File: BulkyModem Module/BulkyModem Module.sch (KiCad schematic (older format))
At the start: 13 parts, among them M1 Mounting, M2 Mounting, M3 Mounting, M4 Mounting, U1 74HCT244, U2 74HCT04

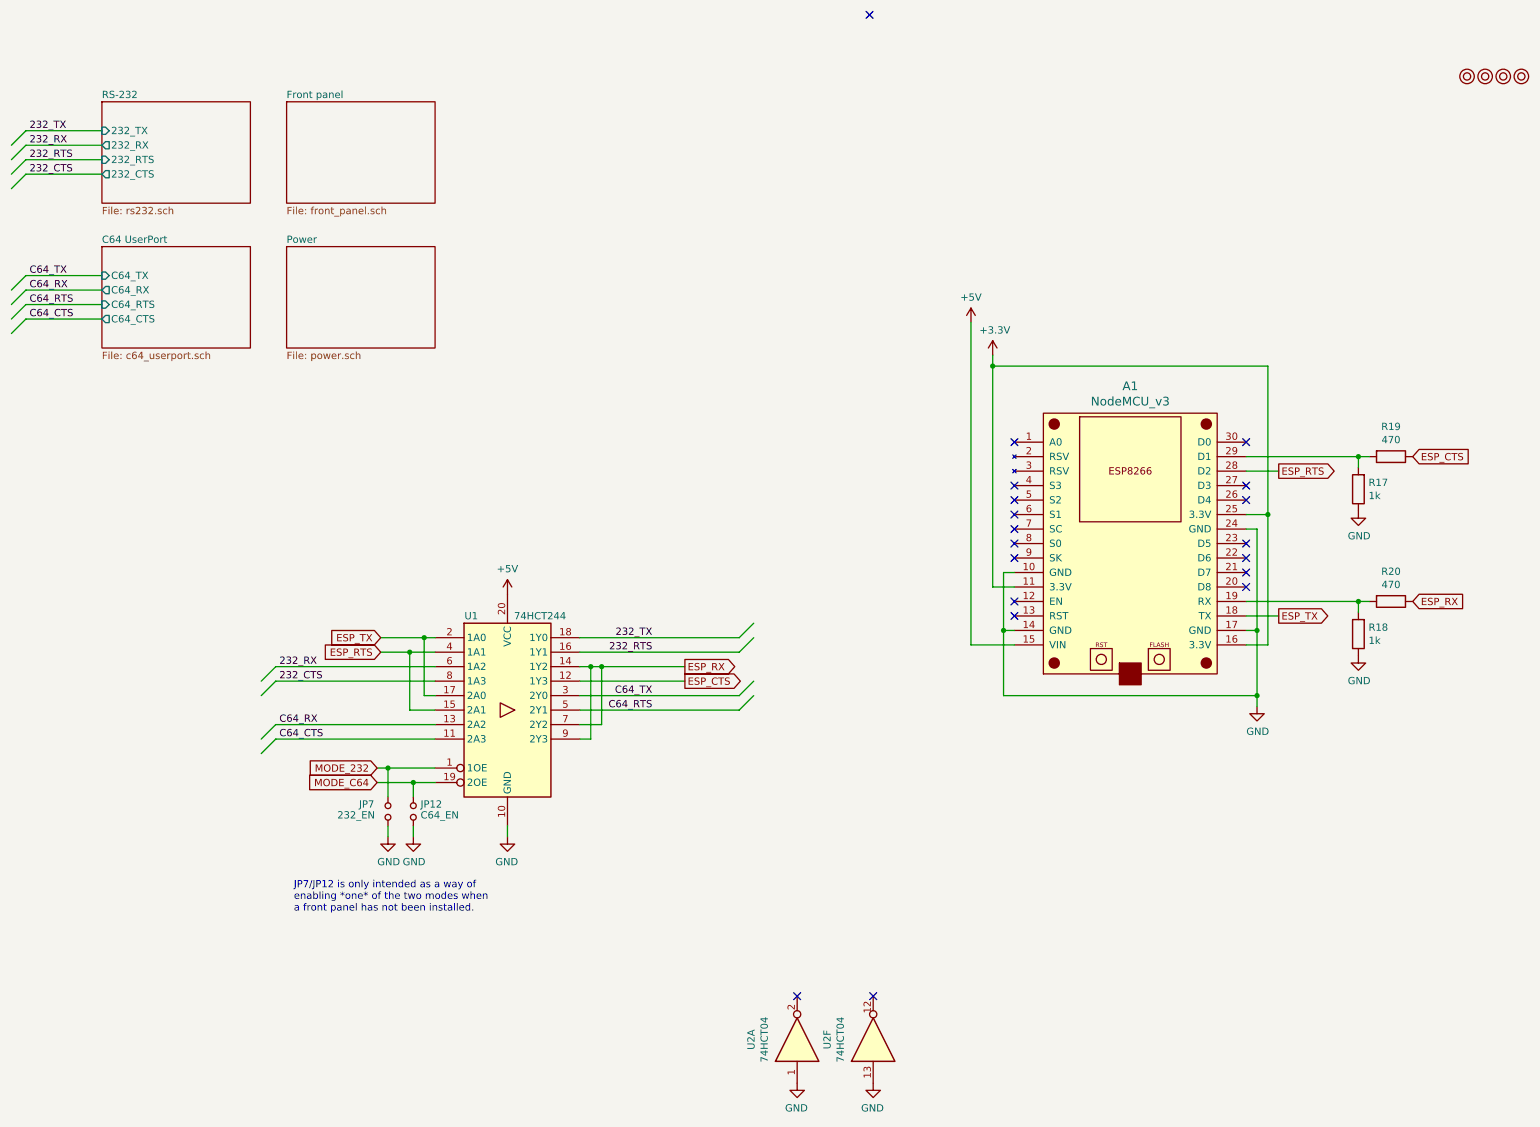
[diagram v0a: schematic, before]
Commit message: C64 UserPort adapter sketched out (preliminary layout)
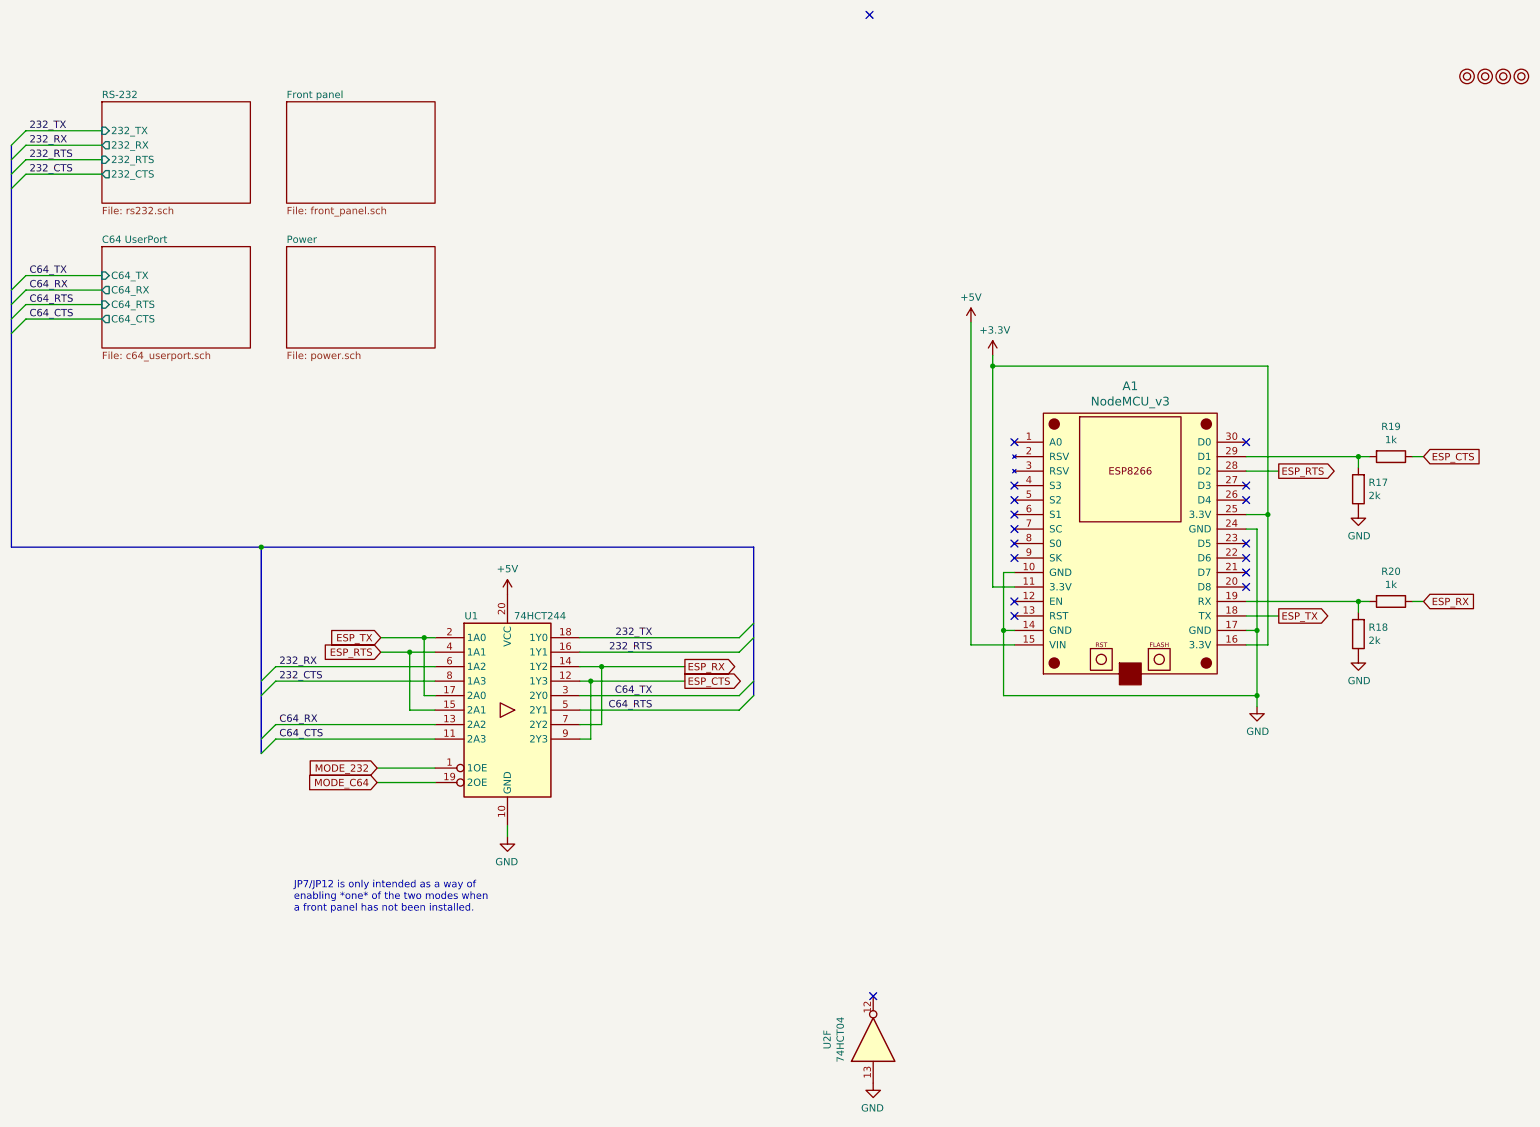
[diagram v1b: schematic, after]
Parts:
- removed JP12: C64_EN, symbol Device:Jumper_NO_Small
- removed JP7: 232_EN, symbol Device:Jumper_NO_Small
- removed unit 1 of U2
- R17, R18: value 1k -> 2k; footprint (none) -> resistor:R_Axial_DIN0207_L6.3mm_D2.5mm_P10.16mm_Horizontal
- R19, R20: value 470 -> 1k; footprint (none) -> resistor:R_Axial_DIN0207_L6.3mm_D2.5mm_P10.16mm_Horizontal
- U1: footprint (none) -> Package_DIP:DIP-20_W7.62mm_Socket_LongPads
- U2: footprint (none) -> Package_DIP:DIP-14_W7.62mm_Socket_LongPads
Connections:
- net ESP_CTS: now also U1.9 (2Y3)
- net ESP_RX: no longer U1.9 (2Y3)
- no-connect marks 19 -> 18
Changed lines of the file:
@@
 F 0 "A1" H 8425 4887 60  0000 C CNN
 F 1 "NodeMCU_v3" H 8425 4781 60  0000 C CNN
-F 2 "" H 7825 2950 60  0000 C CNN
+F 2 "" H 7825 2950 60  0001 C CNN
 F 3 "" H 7825 2950 60  0000 C CNN
 	1    8425 3800
@@
 Wire Wire Line
 	9225 4300 9450 4300
-Text GLabel 10375 4200 2    50   Input ~ 0
+Text GLabel 10450 4200 2    50   Input ~ 0
 ESP_RX
 $Comp
@@
 F 0 "U1" H 3875 5600 50  0000 C CNN
 F 1 "74HCT244" H 4350 5600 50  0000 C CNN
-F 2 "" H 4125 4950 50  0001 C CNN
+F 2 "Package_DIP:DIP-20_W7.62mm_Socket_LongPads" H 4125 4950 50  0001 C CNN
 F 3 "https://assets.nexperia.com/documents/data-sheet/74HC_HCT244.pdf" H 4125 4950 50  0001 C CNN
 	1    4125 4950
@@
 $Comp
 L 74xx:74HCT04 U2
-U 1 1 62F91C25
-P 6125 7225
-F 0 "U2" H 6125 7542 50  0000 C CNN
-F 1 "74HCT04" H 6125 7451 50  0000 C CNN
-F 2 "" H 6125 7225 50  0001 C CNN
-F 3 "https://assets.nexperia.com/documents/data-sheet/74HC_HCT04.pdf" H 6125 7225 50  0001 C CNN
-	1    6125 7225
-	0    -1   -1   0
-$EndComp
-$Comp
-L 74xx:74HCT04 U2
 U 6 1 62F95922
 P 6650 7225
 F 0 "U2" H 6650 7542 50  0000 C CNN
 F 1 "74HCT04" H 6650 7451 50  0000 C CNN
-F 2 "" H 6650 7225 50  0001 C CNN
+F 2 "Package_DIP:DIP-14_W7.62mm_Socket_LongPads" H 6650 7225 50  0001 C CNN
 F 3 "https://assets.nexperia.com/documents/data-sheet/74HC_HCT04.pdf" H 6650 7225 50  0001 C CNN
 	6    6650 7225
 	0    -1   -1   0
 $EndComp
-Text GLabel 10375 3200 2    50   Input ~ 0
+Text GLabel 10450 3200 2    50   Input ~ 0
 ESP_CTS
 Text GLabel 9450 3300 2    50   Output ~ 0
@@
 	9225 3300 9450 3300
 NoConn ~ 6650 6925
-NoConn ~ 6125 6925
 $Sheet
 S 1325 750  1025 700
@@
 	2525 5150 3625 5150
 Wire Wire Line
-	4625 4750 5350 4750
-Wire Wire Line
-	4625 4650 4700 4650
-Wire Wire Line
-	4700 4650 4700 5150
+	4625 4750 4700 4750
 Wire Wire Line
 	4625 5150 4700 5150
-Connection ~ 4700 4650
-Wire Wire Line
-	4775 5050 4775 4650
-Connection ~ 4775 4650
-Wire Wire Line
-	4775 4650 5350 4650
-Wire Wire Line
-	4700 4650 4775 4650
 Wire Wire Line
 	4625 5050 4775 5050
@@
 AR Path="/63E1B523" Ref="R19"  Part="1"
 F 0 "R19" V 10018 3200 50  0000 C CNN
-F 1 "470" V 10109 3200 50  0000 C CNN
-F 2 "" V 10155 3200 50  0001 C CNN
+F 1 "1k" V 10109 3200 50  0000 C CNN
+F 2 "resistor:R_Axial_DIN0207_L6.3mm_D2.5mm_P10.16mm_Horizontal" V 10155 3200 50  0001 C CNN
 F 3 "~" H 10225 3200 50  0001 C CNN
 	1    10225 3200
@@
 AR Path="/63E1D8A2" Ref="R20"  Part="1"
 F 0 "R20" V 10018 4200 50  0000 C CNN
-F 1 "470" V 10109 4200 50  0000 C CNN
-F 2 "" V 10155 4200 50  0001 C CNN
+F 1 "1k" V 10109 4200 50  0000 C CNN
+F 2 "resistor:R_Axial_DIN0207_L6.3mm_D2.5mm_P10.16mm_Horizontal" V 10155 4200 50  0001 C CNN
 F 3 "~" H 10225 4200 50  0001 C CNN
 	1    10225 4200
@@
 AR Path="/63E1DF8E" Ref="R17"  Part="1"
 F 0 "R17" H 9930 3379 50  0000 R CNN
-F 1 "1k" H 9930 3470 50  0000 R CNN
-F 2 "" V 9930 3425 50  0001 C CNN
+F 1 "2k" H 9930 3470 50  0000 R CNN
+F 2 "resistor:R_Axial_DIN0207_L6.3mm_D2.5mm_P10.16mm_Horizontal" V 9930 3425 50  0001 C CNN
 F 3 "~" H 10000 3425 50  0001 C CNN
 	1    10000 3425
@@
 AR Path="/63E2105A" Ref="R18"  Part="1"
 F 0 "R18" H 9930 4379 50  0000 R CNN
-F 1 "1k" H 9930 4470 50  0000 R CNN
-F 2 "" V 9930 4425 50  0001 C CNN
+F 1 "2k" H 9930 4470 50  0000 R CNN
+F 2 "resistor:R_Axial_DIN0207_L6.3mm_D2.5mm_P10.16mm_Horizontal" V 9930 4425 50  0001 C CNN
 F 3 "~" H 10000 4425 50  0001 C CNN
 	1    10000 4425
@@
 $EndComp
 Wire Wire Line
-	3475 5750 3475 5825
-$Comp
-L Device:Jumper_NO_Small JP12
-U 1 1 63E334A2
-P 3475 5650
-AR Path="/63E334A2" Ref="JP12"  Part="1"
-AR Path="/63D786E4/63E334A2" Ref="JP?"  Part="1"
-F 0 "JP12" V 3525 5600 50  0000 R CNN
-F 1 "C64_EN" V 3450 5600 50  0000 R CNN
-F 2 "" H 3475 5650 50  0001 C CNN
-F 3 "~" H 3475 5650 50  0001 C CNN
-	1    3475 5650
-	0    -1   -1   0
-$EndComp
-Wire Wire Line
-	3300 5750 3300 5825
-$Comp
-L Device:Jumper_NO_Small JP7
-U 1 1 63E3925D
-P 3300 5650
-AR Path="/63E3925D" Ref="JP7"  Part="1"
-AR Path="/63D786E4/63E3925D" Ref="JP?"  Part="1"
-F 0 "JP7" V 3350 5850 50  0000 R CNN
-F 1 "232_EN" V 3275 6000 50  0000 R CNN
-F 2 "" H 3300 5650 50  0001 C CNN
-F 3 "~" H 3300 5650 50  0001 C CNN
-	1    3300 5650
-	0    -1   -1   0
-$EndComp
-$Comp
-L power:GND #PWR04
-U 1 1 63E3349C
-P 3475 5825
-AR Path="/63E3349C" Ref="#PWR04"  Part="1"
-AR Path="/63D786E4/63E3349C" Ref="#PWR?"  Part="1"
-F 0 "#PWR04" H 3475 5575 50  0001 C CNN
-F 1 "GND" H 3480 5652 50  0000 C CNN
-F 2 "" H 3475 5825 50  0001 C CNN
-F 3 "" H 3475 5825 50  0001 C CNN
-	1    3475 5825
-	1    0    0    -1
-$EndComp
-$Comp
-L power:GND #PWR02
-U 1 1 63E39257
-P 3300 5825
-AR Path="/63E39257" Ref="#PWR02"  Part="1"
-AR Path="/63D786E4/63E39257" Ref="#PWR?"  Part="1"
-F 0 "#PWR02" H 3300 5575 50  0001 C CNN
-F 1 "GND" H 3305 5652 50  0000 C CNN
-F 2 "" H 3300 5825 50  0001 C CNN
-F 3 "" H 3300 5825 50  0001 C CNN
-	1    3300 5825
-	1    0    0    -1
-$EndComp
-Wire Wire Line
 	4125 5825 4125 5750
-Wire Wire Line
-	3300 5550 3300 5350
-Wire Wire Line
-	3300 5350 3625 5350
-Wire Wire Line
-	3225 5350 3300 5350
-Connection ~ 3300 5350
-Wire Wire Line
-	3225 5450 3475 5450
-Wire Wire Line
-	3475 5450 3475 5550
-Connection ~ 3475 5450
-Wire Wire Line
-	3475 5450 3625 5450
-$Comp
-L power:GND #PWR0137
-U 1 1 63E5BB2D
-P 6125 7525
-F 0 "#PWR0137" H 6125 7275 50  0001 C CNN
-F 1 "GND" H 6130 7352 50  0000 C CNN
-F 2 "" H 6125 7525 50  0001 C CNN
-F 3 "" H 6125 7525 50  0001 C CNN
-	1    6125 7525
-	-1   0    0    -1
-$EndComp
 $Comp
 L power:GND #PWR0138
@@
 Text Notes 2650 6350 0    50   ~ 0
 JP7/JP12 is only intended as a way of\nenabling *one* of the two modes when\na front panel has not been installed.
+Wire Wire Line
+	4625 4650 4775 4650
+Wire Wire Line
+	4700 5150 4700 4750
+Connection ~ 4700 4750
+Wire Wire Line
+	4700 4750 5350 4750
+Wire Wire Line
+	4775 5050 4775 4650
+Connection ~ 4775 4650
+Wire Wire Line
+	4775 4650 5350 4650
+Wire Bus Line
+	2425 3825 5825 3825
+Wire Bus Line
+	700  3825 2425 3825
+Connection ~ 2425 3825
+Wire Wire Line
+	3225 5450 3625 5450
+Wire Wire Line
+	3225 5350 3625 5350
+Wire Wire Line
+	10450 4200 10375 4200
+Wire Wire Line
+	10375 3200 10450 3200
+Wire Bus Line
+	2425 3825 2425 5250
+Wire Bus Line
+	5825 3825 5825 4850
+Wire Bus Line
+	700  1050 700  3825
 $EndSCHEMATC

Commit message: Add MCU footprints
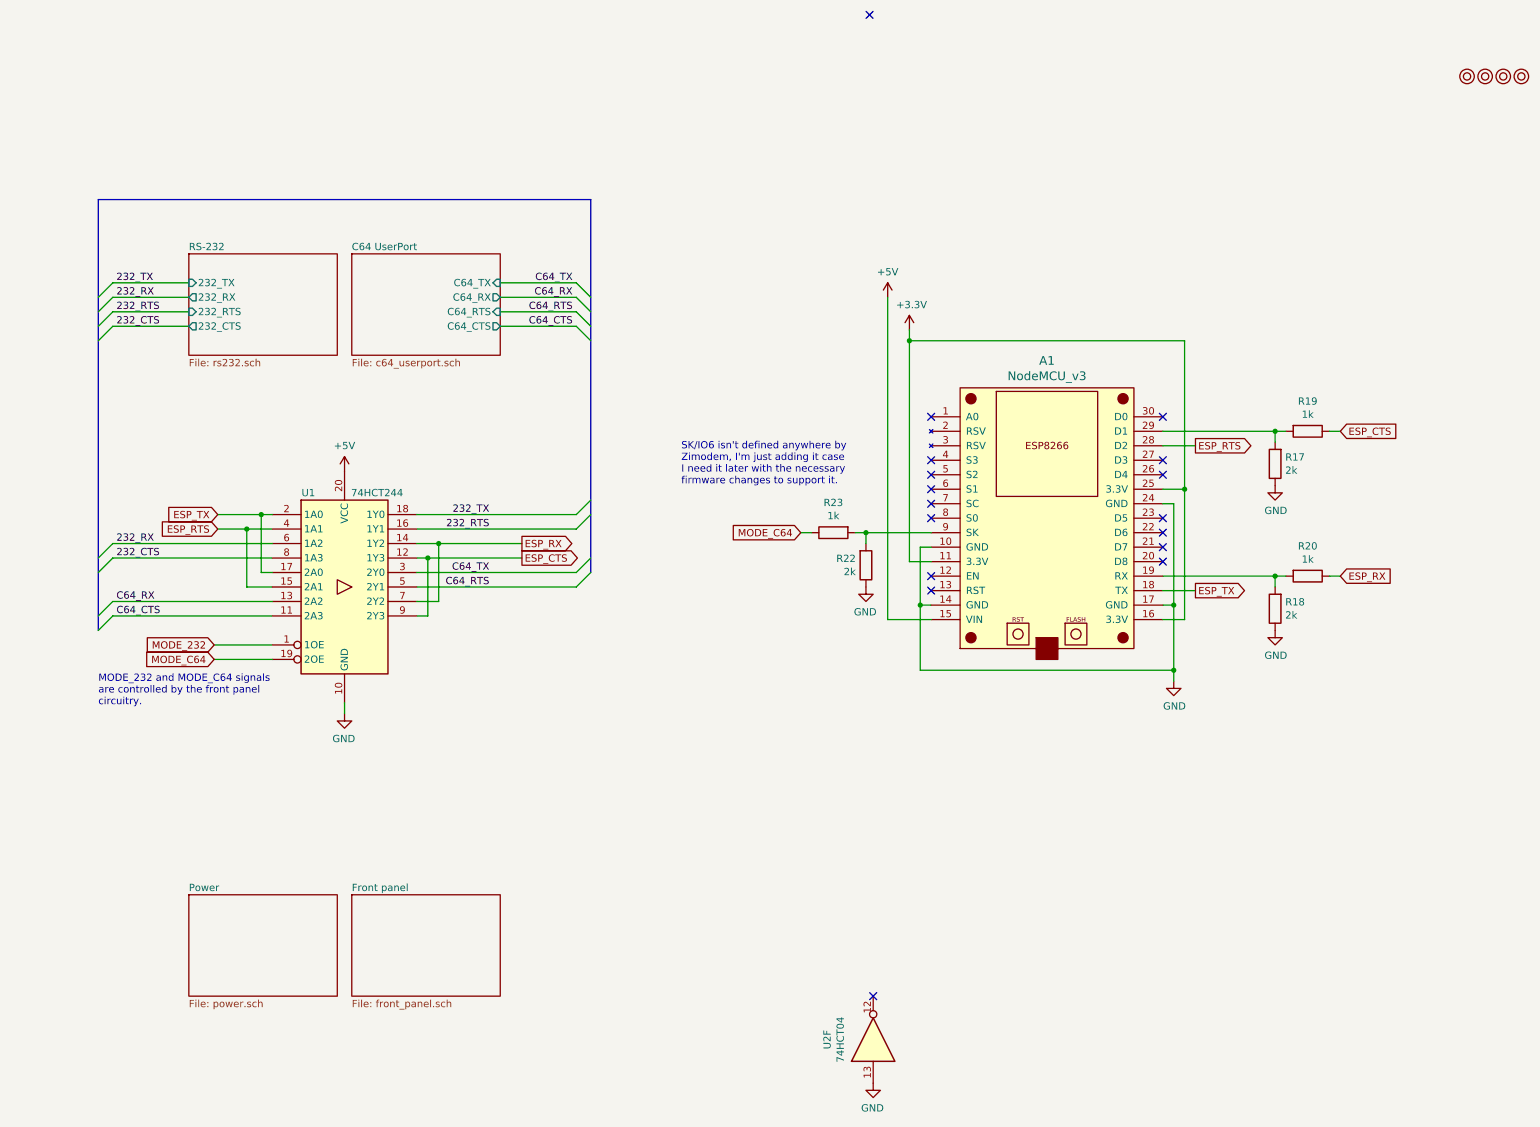
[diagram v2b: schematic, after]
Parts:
- added R22: 2k, resistor:R_Axial_DIN0207_L6.3mm_D2.5mm_P10.16mm_Horizontal, symbol Device:R
- added R23: 1k, resistor:R_Axial_DIN0207_L6.3mm_D2.5mm_P10.16mm_Horizontal, symbol Device:R
- A1: footprint (none) -> nodemcu_v3:NodeMCU-LoLinV3
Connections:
- net GND: now also R22.1
- net MODE_C64: now also R23.1
- net at A1.9 (SK): now also R22.2, R23.2
- no-connect marks 18 -> 17
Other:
- note added: "MODE_232 and MODE_C64 signals\nare controlled by the front panel\ncircuitry."
- note added: "SK/IO6 isn't defined anywhere by\nZimodem, I'm just adding it case\nI need it later with the necessary\nfirmware changes to support it."
- note removed: "JP7/JP12 is only intended as a way of\nenabling *one* of the two modes when\na front panel has not been installed."
- moved on the sheet: A1, R17, R18, R19, R20, U1

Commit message: Add DCD
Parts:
- removed U2: 74HCT04, Package_DIP:DIP-14_W7.62mm_Socket_LongPads, symbol 74xx:74HCT04
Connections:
- net ESP_DCD: now reaches A1.26 (D4)
- no-connect marks 17 -> 15
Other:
- note added: "Note that the DCD signal is shared between the two, something I'll\n"probably" get away with since they are only outgoing signals. The\n232 side will get buffered by the inverter used."
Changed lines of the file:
@@
 	-1   0    0    -1
-$EndComp
-$Comp
-L 74xx:74HCT04 U2
-U 6 1 62F95922
-P 6650 7225
-F 0 "U2" H 6650 7542 50  0000 C CNN
-F 1 "74HCT04" H 6650 7451 50  0000 C CNN
-F 2 "Package_DIP:DIP-14_W7.62mm_Socket_LongPads" H 6650 7225 50  0001 C CNN
-F 3 "https://assets.nexperia.com/documents/data-sheet/74HC_HCT04.pdf" H 6650 7225 50  0001 C CNN
-	6    6650 7225
-	0    -1   -1   0
 $EndComp
 Text GLabel 9875 3025 2    50   Input ~ 0
@@
 Wire Wire Line
 	8650 3125 8875 3125
-NoConn ~ 6650 6925
 $Sheet
 S 1925 1800 1025 700
@@
 F4 "232_CTS" O L 1925 2300 50
 F5 "232_RTS" I L 1925 2200 50
+F6 "232_DCD" I L 1925 2400 50
 $EndSheet
 $Sheet
@@
 F4 "C64_TX" I R 4075 2000 50
 F5 "C64_RTS" I R 4075 2200 50
+F6 "C64_DCD" I R 4075 2400 50
 $EndSheet
 Wire Wire Line
@@
 Wire Wire Line
 	3000 4975 3000 4900
-$Comp
-L power:GND #PWR0138
-U 1 1 63E5C8FB
-P 6650 7525
-F 0 "#PWR0138" H 6650 7275 50  0001 C CNN
-F 1 "GND" H 6655 7352 50  0000 C CNN
-F 2 "" H 6650 7525 50  0001 C CNN
-F 3 "" H 6650 7525 50  0001 C CNN
-	1    6650 7525
-	-1   0    0    -1
-$EndComp
 Wire Wire Line
 	3500 4000 4600 4000
@@
 Wire Wire Line
 	6600 3725 7050 3725
-NoConn ~ 8650 3325
 Wire Wire Line
 	8650 3025 9425 3025
@@
 Wire Bus Line
 	1300 1425 4700 1425
+Text Notes 1300 4925 0    50   ~ 0
+MODE_232 and MODE_C64 signals\nare controlled by the front panel\ncircuitry.
+Text GLabel 8875 3325 2    50   Output ~ 0
+ESP_DCD
+Wire Wire Line
+	8650 3325 8875 3325
+Text GLabel 1850 2400 0    50   Input ~ 0
+ESP_DCD
+Wire Wire Line
+	1850 2400 1925 2400
+Text GLabel 4150 2400 2    50   Input ~ 0
+ESP_DCD
+Wire Wire Line
+	4150 2400 4075 2400
+Text Notes 1725 2900 0    50   ~ 0
+Note that the DCD signal is shared between the two, something I'll\n"probably" get away with since they are only outgoing signals. The\n232 side will get buffered by the inverter used.
 Wire Bus Line
 	4700 1425 4700 4000
 Wire Bus Line
 	1300 1425 1300 4400
-Text Notes 1300 4925 0    50   ~ 0
-MODE_232 and MODE_C64 signals\nare controlled by the front panel\ncircuitry.
 $EndSCHEMATC
